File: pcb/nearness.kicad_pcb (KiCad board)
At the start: 2 copper layers, 39.4 x 106.7 mm, 52 parts, among them J1 PJ301M12, J2 PJ301M12, J3 PJ301M12, J4 PJ301M12, J5 PJ301M12, J6 PJ301M12, J7 PJ301M12, J8 PJ301M12, J9 PJ301M12, P1 CONN_01X05, P2 CONN_01X05, P3 CONN_01X05, P4 CONN_01X05, P5 CONN_01X03, P6 CONN_01X03, P7 CONN_01X03, U1 LME49720, U2 LME49720

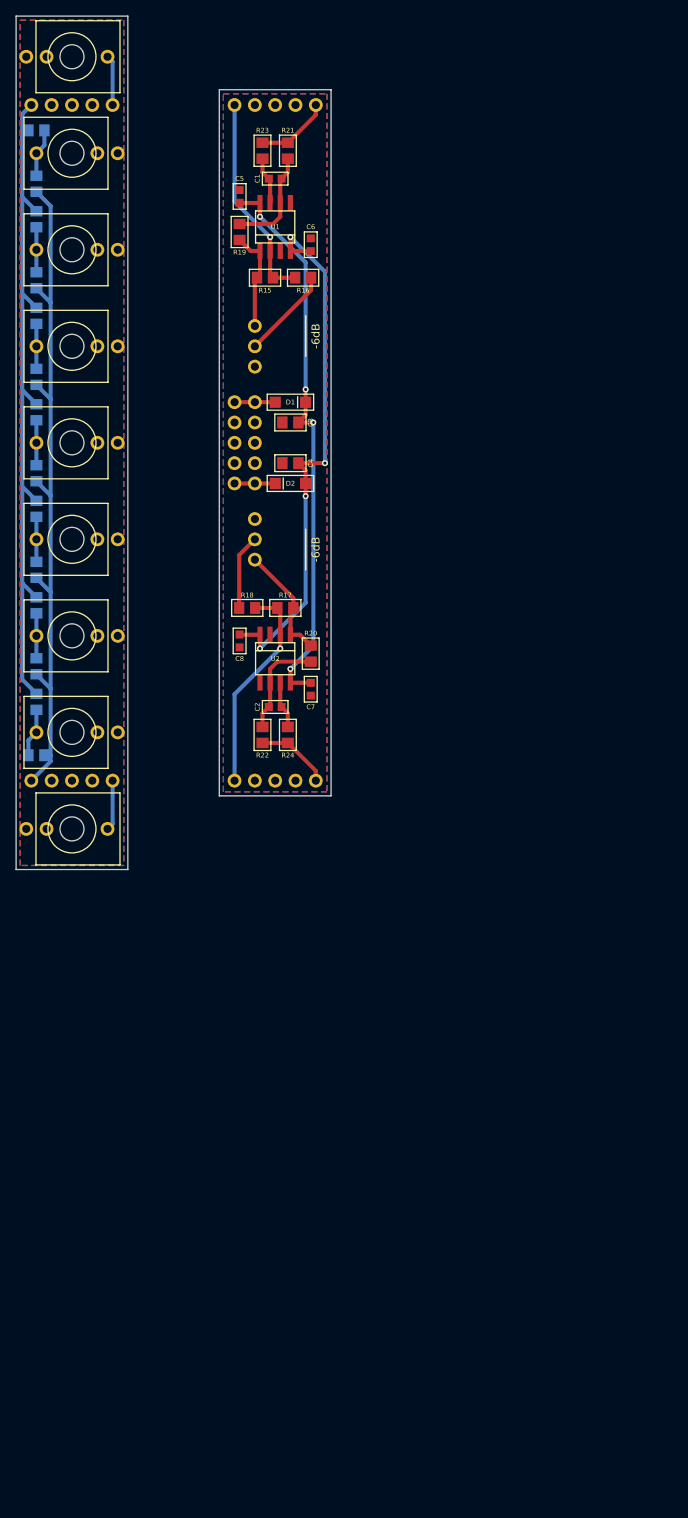
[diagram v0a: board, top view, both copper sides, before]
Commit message: Updated symbols and silkscreen
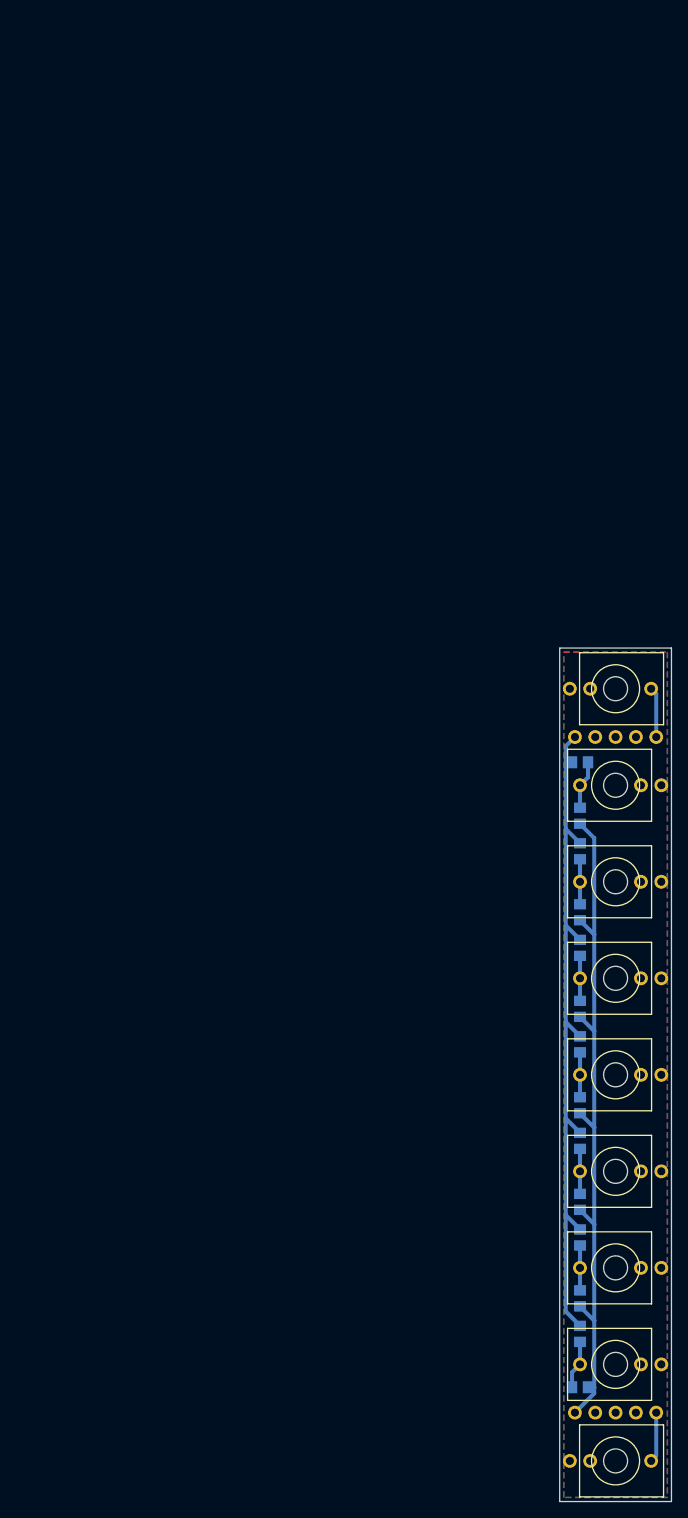
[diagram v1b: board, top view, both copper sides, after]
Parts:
- removed C1, C2: 22p, nearness:0603
- removed C3, C4: 22u, nearness:0805
- removed C5, C6, C7, C8: 100n, nearness:0603
- removed D1, D2: 1N5819HW, nearness:SOD-123
- removed P3, P4: CONN_01X05, nearness:Pin_1x5
- removed P5, P6: CONN_01X03, nearness:Pin_1x3
- removed P7: CONN_01X03, nearness:Eurorack_2x5
- removed R15, R16, R17, R18, R19, R20, R21, R22: 100k, nearness:0805
- removed R23, R24: 1k, nearness:0805
- removed U1, U2: LME49720, nearness:SOIC-8
- moved J1 104.2 mm to (68.0, 30.7)
- moved J2 104.2 mm to (68.0, 42.8)
- moved J3 104.2 mm to (68.0, 54.9)
- moved J4 104.2 mm to (68.0, 66.9)
- moved J5 104.2 mm to (68.0, 79.0)
- moved J6 104.2 mm to (68.0, 91.1)
- moved J7 104.2 mm to (68.0, 103.1)
- moved J8 104.2 mm to (68.0, 115.2)
- moved J9 104.2 mm to (68.0, 127.3)
- moved P1 104.2 mm to (68.0, 36.8)
- moved P2 104.2 mm to (68.0, 121.2)
- moved R1 104.2 mm to (63.5, 39.9)
- moved R10 104.2 mm to (63.5, 94.9)
- moved R11 104.2 mm to (63.5, 99.3)
- moved R12 104.2 mm to (63.5, 106.9)
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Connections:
- J1 pad 2: Net-(J1-Pad2) -> (no net)
- J9 pad 2: Net-(J9-Pad2) -> (no net)
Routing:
- net +12V: track 70.8 -> 0.00 mm, vias 4 -> 0
- net -12V: track 67.8 -> 0.00 mm, vias 4 -> 0
- net Net-(P4-Pad1): track 26.9 -> 0.00 mm, vias 1 -> 0
- net Net-(P3-Pad1): track 26.3 -> 0.00 mm, vias 1 -> 0
- net Net-(P6-Pad1): track 14.6 -> 0.00 mm
- net Net-(C1-Pad1): track 13.1 -> 0.00 mm
- net Net-(C2-Pad1): track 13.1 -> 0.00 mm
- net Net-(P5-Pad1): track 12.8 -> 0.00 mm
- net Net-(P5-Pad2): track 11.5 -> 0.00 mm
- net Net-(P6-Pad2): track 9.38 -> 0.00 mm
- net Net-(P4-Pad5): track 9.34 -> 0.00 mm
- net Net-(P3-Pad5): track 9.34 -> 0.00 mm
- net Net-(C2-Pad2): track 5.92 -> 0.00 mm
- net Net-(C1-Pad2): track 5.92 -> 0.00 mm
- net Net-(D2-Pad1): track 5.09 -> 0.00 mm
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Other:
- board size 39.4 x 106.7 mm -> 14 x 106.7 mm
- board text removed: "-6dB"
